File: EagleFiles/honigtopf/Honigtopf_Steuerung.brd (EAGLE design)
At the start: 71.1 x 58.4 mm, 12 parts

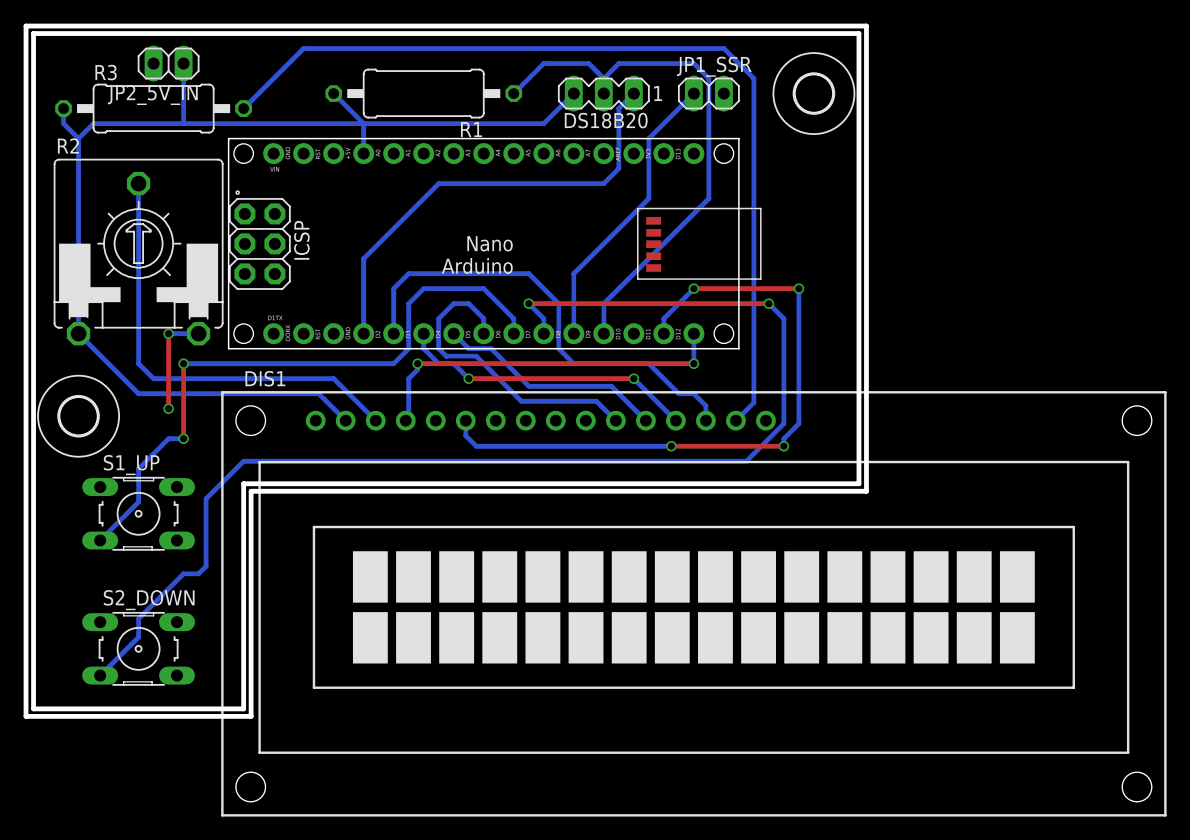
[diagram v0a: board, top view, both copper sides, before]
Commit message: changed standard temp to 39
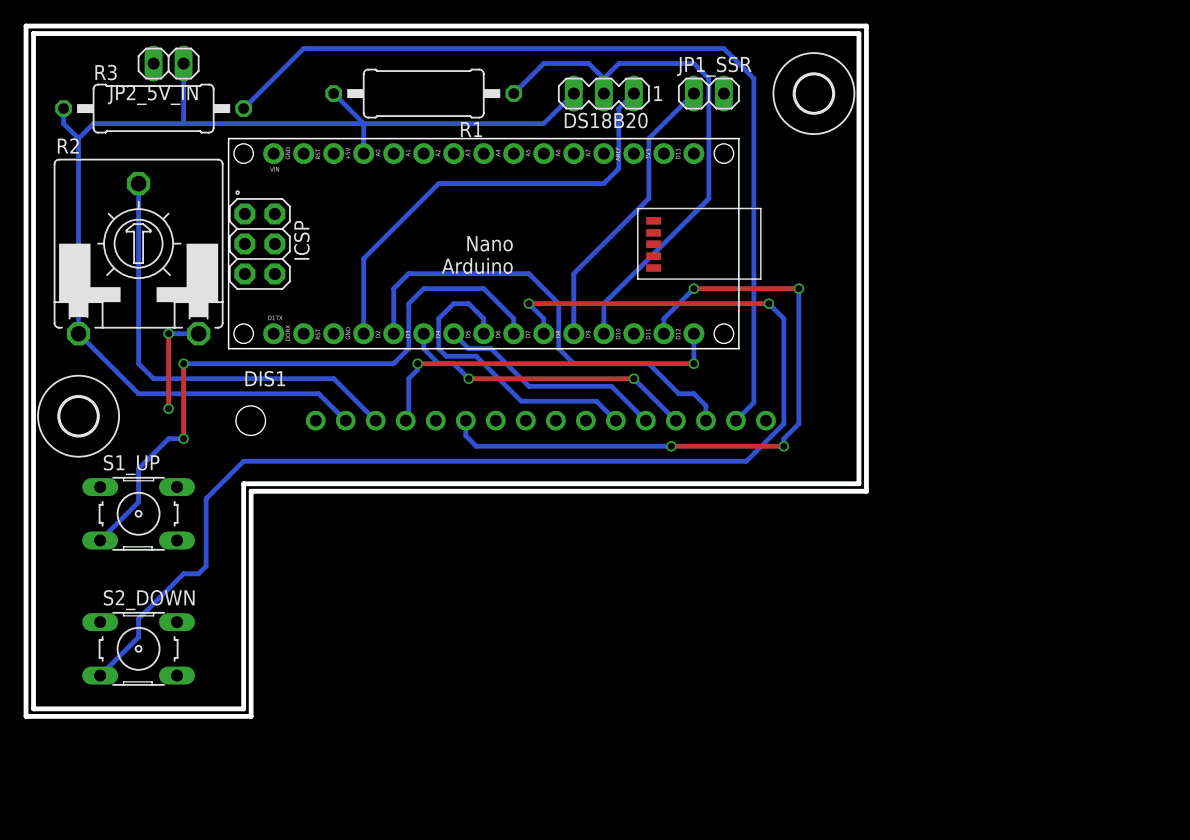
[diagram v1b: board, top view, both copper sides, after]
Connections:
- net GND: now also JP1_SSR.2
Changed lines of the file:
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@@
 <via x="10.16" y="48.26" extent="1-16" drill="0.6" shape="square"/>
 <contactref element="JP2_5V_IN" pad="2"/>
+<contactref element="JP1_SSR" pad="2"/>
+<wire x1="49.53" y1="74.93" x2="57.15" y2="74.93" width="0" layer="19" extent="1-1"/>
 </signal>
 <signal name="5V">
